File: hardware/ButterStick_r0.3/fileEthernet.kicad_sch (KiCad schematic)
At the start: 46 parts, among them CON1 JD1_0001NL, U2 KSZ9031, Y1 25Mhz

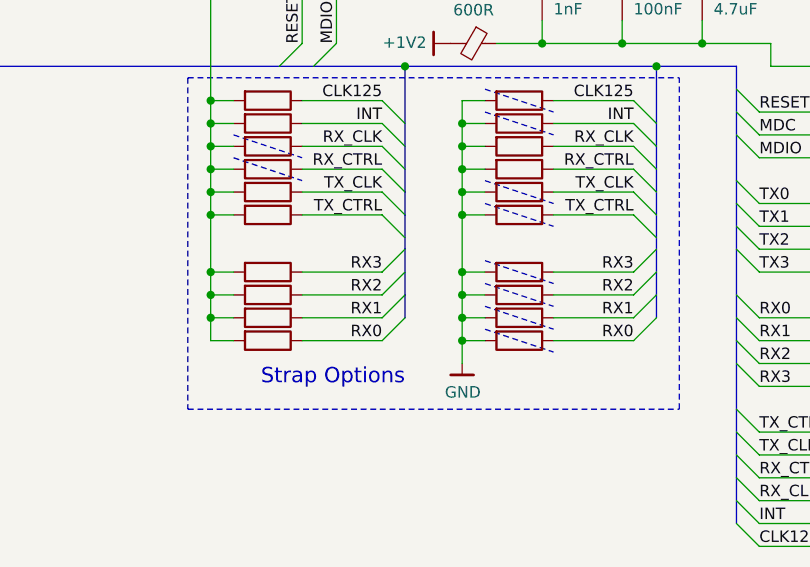
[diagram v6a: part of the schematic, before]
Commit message: hw.r0d3: update routing
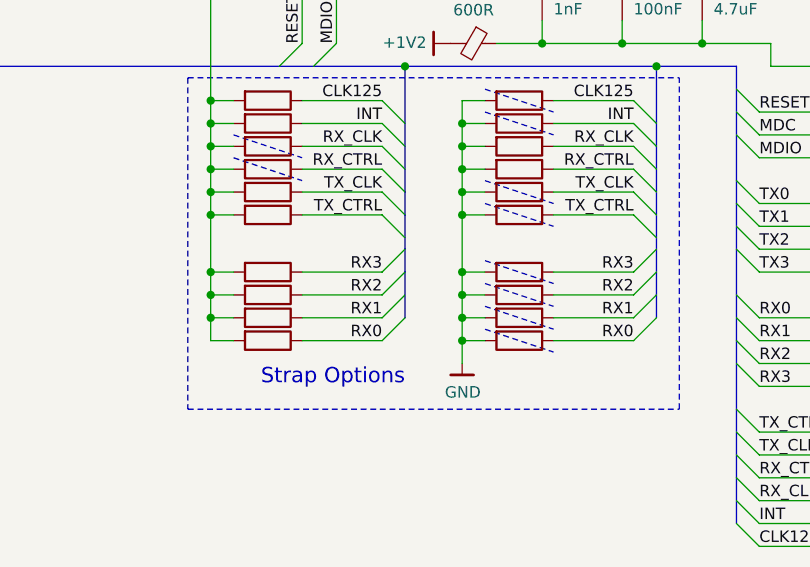
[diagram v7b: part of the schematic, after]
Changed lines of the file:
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@@
   (junction (at 83.82 91.44))
   (junction (at 111.76 91.44))
+  (no_connect (at 194.31 100.33))
   (no_connect (at 194.31 102.87))
-  (no_connect (at 194.31 100.33))
   (bus_entry (at 72.39 88.9) (size -2.54 2.54))
   (bus_entry (at 76.2 88.9) (size -2.54 2.54))
@@
     (stroke (width 0) (type solid) (color 0 0 0 0))
   )
-  (bus (pts (xy 83.82 111.76) (xy 83.82 116.84))
-    (stroke (width 0) (type solid) (color 0 0 0 0))
-  )
-  (bus (pts (xy 83.82 116.84) (xy 83.82 119.38))
-    (stroke (width 0) (type solid) (color 0 0 0 0))
-  )
+  (bus (pts (xy 83.82 111.76) (xy 83.82 114.3))
+    (stroke (width 0) (type solid) (color 0 0 0 0))
+  )
+  (bus (pts (xy 83.82 114.3) (xy 83.82 119.38))
+    (stroke (width 0) (type solid) (color 0 0 0 0))
+  )

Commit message: hw.r0d3: Continue routing
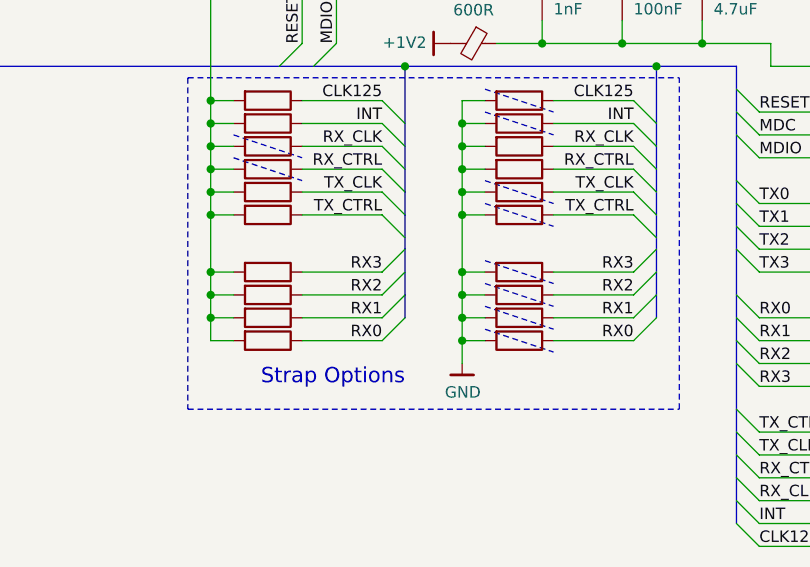
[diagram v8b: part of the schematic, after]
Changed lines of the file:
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@@
     (stroke (width 0) (type solid) (color 0 0 0 0))
   )
-  (bus (pts (xy 83.82 111.76) (xy 83.82 114.3))
+  (bus (pts (xy 83.82 111.76) (xy 83.82 116.84))
     (stroke (width 0) (type solid) (color 0 0 0 0))
   )
-  (bus (pts (xy 83.82 114.3) (xy 83.82 119.38))
+  (bus (pts (xy 83.82 116.84) (xy 83.82 119.38))
     (stroke (width 0) (type solid) (color 0 0 0 0))
   )
